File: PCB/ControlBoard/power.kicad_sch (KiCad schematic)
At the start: 26 parts, among them J10 BUSPWR, U5 TPS629210, U6 TPS629210

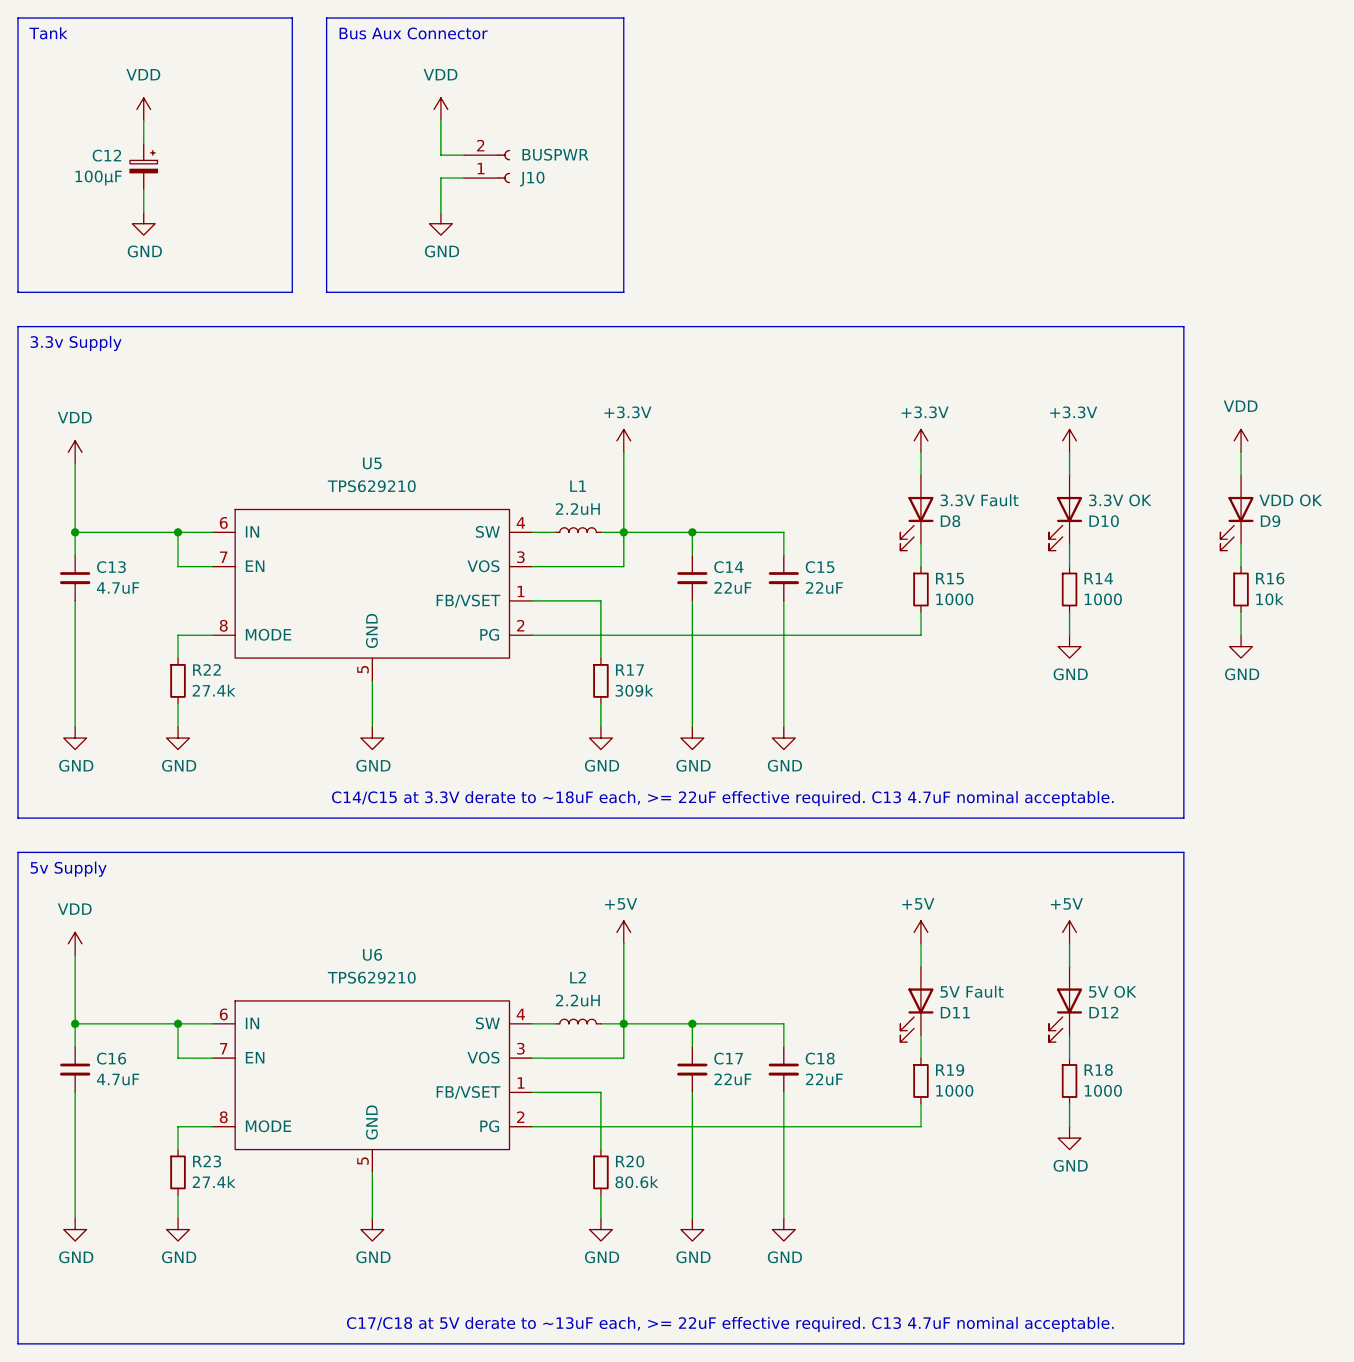
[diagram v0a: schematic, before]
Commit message: feat: Rework ControlBoard to use an STM32H562VGT6.
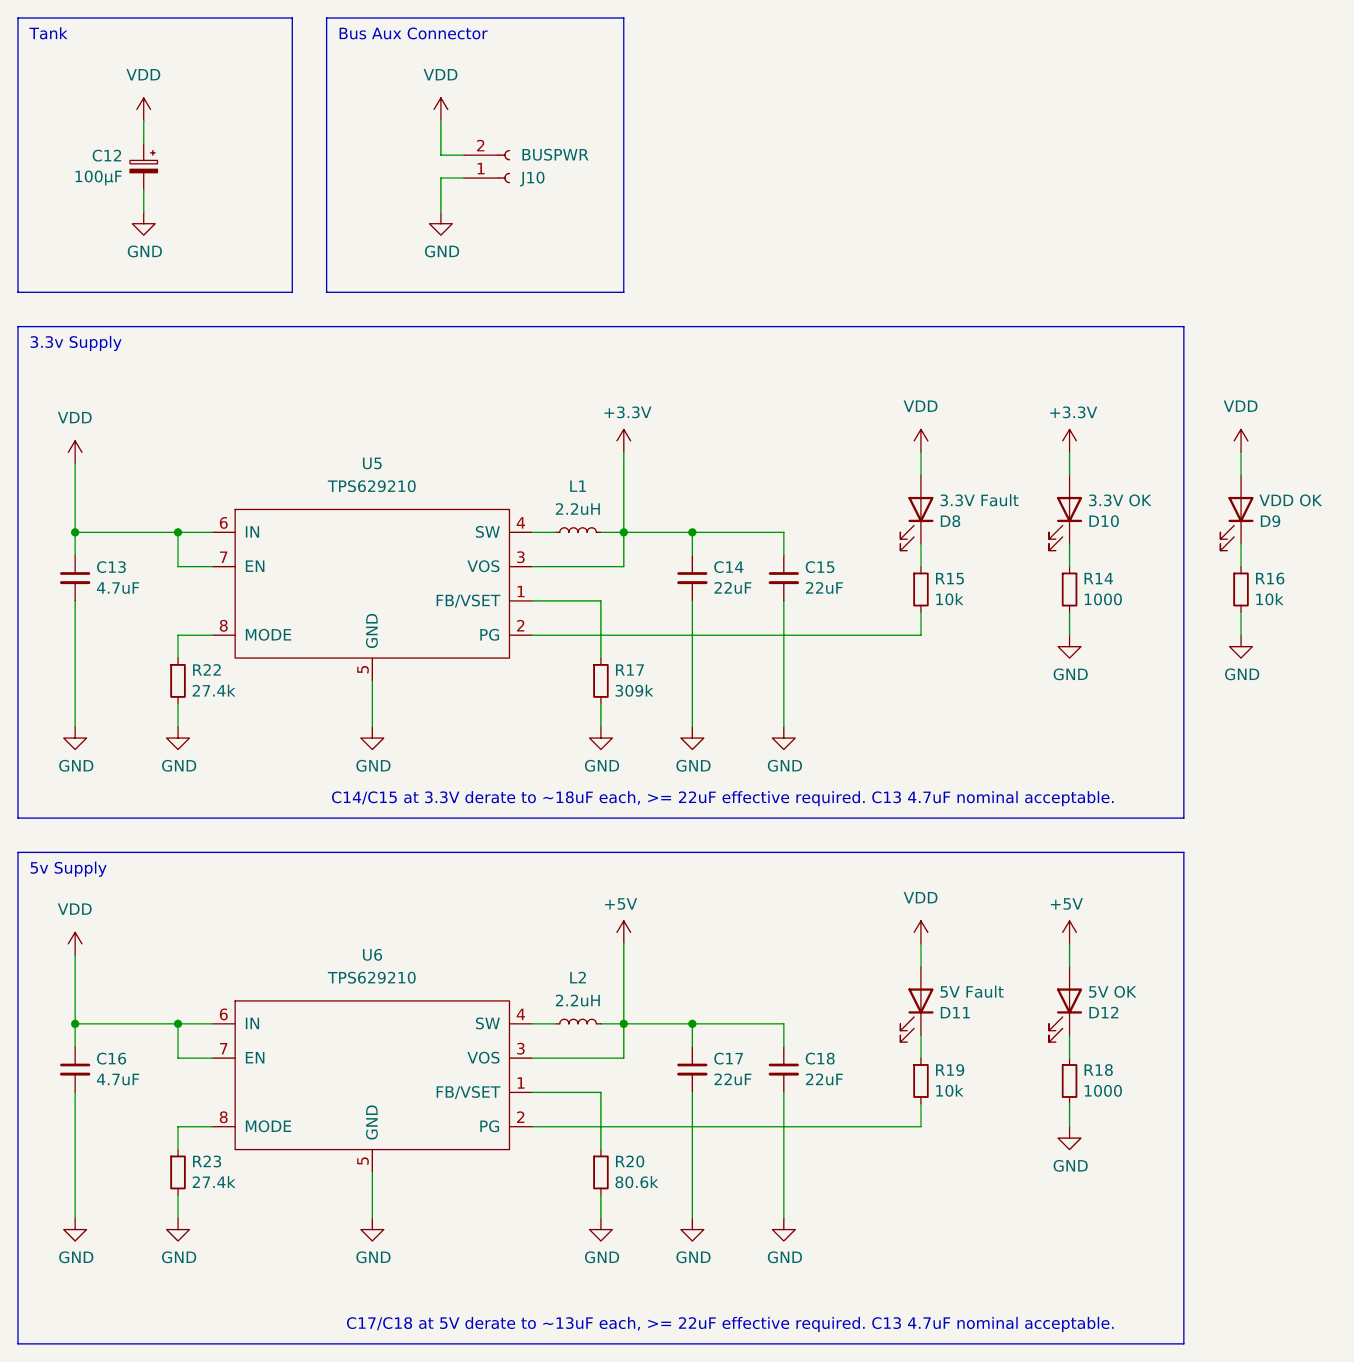
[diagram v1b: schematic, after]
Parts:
- R15, R19: value 1000 -> 10k; DIGIKEY P1.00KHCT-ND -> P10.0KHCT-ND
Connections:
- net +3.3V: no longer D8.2 (A)
- net +5V: no longer D11.2 (A)
- net VDD: now also D11.2 (A), D8.2 (A)
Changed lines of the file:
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@@
 			)
 		)
-		(property "Value" "1000"
+		(property "Value" "10k"
 			(at 117.0686 79.883 0)
 			(show_name no)
@@
 			)
 		)
-		(property "DIGIKEY" "P1.00KHCT-ND"
+		(property "DIGIKEY" "P10.0KHCT-ND"
 			(at 115.57 78.74 0)
 			(hide yes)
@@
 	)
 	(symbol
+		(lib_id "power:VDD")
+		(at 115.57 63.5 0)
+		(unit 1)
+		(body_style 1)
+		(exclude_from_sim no)
+		(in_bom yes)
+		(on_board yes)
+		(in_pos_files yes)
+		(dnp no)
+		(fields_autoplaced yes)
+		(property "Reference" "#PWR086"
+			(at 115.57 67.31 0)
+			(hide yes)
+			(show_name no)
+			(do_not_autoplace no)
+			(effects
+				(font
+					(size 1.27 1.27)
+				)
+			)
+		)
+		(property "Value" "VDD"
+			(at 115.57 58.42 0)
+			(show_name no)
+			(do_not_autoplace no)
+			(effects
+				(font
+					(size 1.27 1.27)
+				)
+			)
+		)
+		(property "Footprint" ""
+			(at 115.57 63.5 0)
+			(hide yes)
+			(show_name no)
+			(do_not_autoplace no)
+			(effects
+				(font
+					(size 1.27 1.27)
+				)
+			)
+		)
+		(property "Datasheet" ""
+			(at 115.57 63.5 0)
+			(hide yes)
+			(show_name no)
+			(do_not_autoplace no)
+			(effects
+				(font
+					(size 1.27 1.27)
+				)
+			)
+		)
+		(property "Description" "Power symbol creates a global label with name \"VDD\""
+			(at 115.57 63.5 0)
+			(hide yes)
+			(show_name no)
+			(do_not_autoplace no)
+			(effects
+				(font
+					(size 1.27 1.27)
+				)
+			)
+		)
+		(pin "1"
+		)
+		(instances
+			(project "ControlBoard"
+				(path "/8a650ebf-3f78-4ca4-a26b-a5028693e36d/8aac65e2-4dfd-463b-a6c0-b675e1c87ded"
+					(reference "#PWR086")
+					(unit 1)
+				)
+			)
+		)
+	)
+	(symbol
 		(lib_id "Device:C_Polarized_Small")
 		(at 29.21 31.75 0)
@@
 			)
 		)
-		(property "Value" "1000"
+		(property "Value" "10k"
 			(at 117.0686 134.493 0)
 			(show_name no)
@@
 			)
 		)
-		(property "DIGIKEY" "P1.00KHCT-ND"
+		(property "DIGIKEY" "P10.0KHCT-ND"
 			(at 115.57 133.35 0)
 			(hide yes)
@@
 	)
 	(symbol
-		(lib_id "power:+5V")
-		(at 115.57 118.11 0)
-		(mirror y)
-		(unit 1)
-		(body_style 1)
-		(exclude_from_sim no)
-		(in_bom yes)
-		(on_board yes)
-		(in_pos_files yes)
-		(dnp no)
-		(property "Reference" "#PWR086"
-			(at 115.57 121.92 0)
-			(hide yes)
-			(show_name no)
-			(do_not_autoplace no)
-			(effects
-				(font
-					(size 1.27 1.27)
-				)
-			)
-		)
-		(property "Value" "+5V"
-			(at 115.189 113.7158 0)
-			(show_name no)
-			(do_not_autoplace no)
-			(effects
-				(font
-					(size 1.27 1.27)
-				)
-			)
-		)
-		(property "Footprint" ""
-			(at 115.57 118.11 0)
-			(hide yes)
-			(show_name no)
-			(do_not_autoplace no)
-			(effects
-				(font
-					(size 1.27 1.27)
-				)
-			)
-		)
-		(property "Datasheet" ""
-			(at 115.57 118.11 0)
-			(hide yes)
-			(show_name no)
-			(do_not_autoplace no)
-			(effects
-				(font
-					(size 1.27 1.27)
-				)
-			)
-		)
-		(property "Description" "Power symbol creates a global label with name \"+5V\""
-			(at 115.57 118.11 0)
-			(hide yes)
-			(show_name no)
-			(do_not_autoplace no)
-			(effects
-				(font
-					(size 1.27 1.27)
-				)
-			)
-		)
-		(pin "1"
-		)
-		(instances
-			(project "ControlBoard"
-				(path "/8a650ebf-3f78-4ca4-a26b-a5028693e36d/8aac65e2-4dfd-463b-a6c0-b675e1c87ded"
-					(reference "#PWR086")
-					(unit 1)
-				)
-			)
-		)
-	)
-	(symbol
 		(lib_id "power:GND")
 		(at 132.08 83.82 0)
@@
 	)
 	(symbol
-		(lib_id "power:+3.3V")
-		(at 115.57 63.5 0)
-		(unit 1)
-		(body_style 1)
-		(exclude_from_sim no)
-		(in_bom yes)
-		(on_board yes)
-		(in_pos_files yes)
-		(dnp no)
-		(property "Reference" "#PWR073"
-			(at 115.57 67.31 0)
-			(hide yes)
-			(show_name no)
-			(do_not_autoplace no)
-			(effects
-				(font
-					(size 1.27 1.27)
-				)
-			)
-		)
-		(property "Value" "+3.3V"
-			(at 115.951 59.1058 0)
-			(show_name no)
-			(do_not_autoplace no)
-			(effects
-				(font
-					(size 1.27 1.27)
-				)
-			)
-		)
-		(property "Footprint" ""
-			(at 115.57 63.5 0)
-			(hide yes)
-			(show_name no)
-			(do_not_autoplace no)
-			(effects
-				(font
-					(size 1.27 1.27)
-				)
-			)
-		)
-		(property "Datasheet" ""
-			(at 115.57 63.5 0)
-			(hide yes)
-			(show_name no)
-			(do_not_autoplace no)
-			(effects
-				(font
-					(size 1.27 1.27)
-				)
-			)
-		)
-		(property "Description" "Power symbol creates a global label with name \"+3.3V\""
-			(at 115.57 63.5 0)
-			(hide yes)
-			(show_name no)
-			(do_not_autoplace no)
-			(effects
-				(font
-					(size 1.27 1.27)
-				)
-			)
-		)
-		(pin "1"
-		)
-		(instances
-			(project "ControlBoard"
-				(path "/8a650ebf-3f78-4ca4-a26b-a5028693e36d/8aac65e2-4dfd-463b-a6c0-b675e1c87ded"
-					(reference "#PWR073")
-					(unit 1)
-				)
-			)
-		)
-	)
-	(symbol
 		(lib_id "power:GND")
 		(at 21.59 148.59 0)
@@
 					(unit 1)
 				)
+			)
+		)
+	)
+	(symbol
+		(lib_id "power:VDD")
+		(at 115.57 118.11 0)
+		(unit 1)
+		(body_style 1)
+		(exclude_from_sim no)
+		(in_bom yes)
+		(on_board yes)
+		(in_pos_files yes)
+		(dnp no)
+		(fields_autoplaced yes)
+		(property "Reference" "#PWR097"
+			(at 115.57 121.92 0)
+			(hide yes)
+			(show_name no)
+			(do_not_autoplace no)
+			(effects
+				(font
+					(size 1.27 1.27)
+				)
+			)
+		)
+		(property "Value" "VDD"
+			(at 115.57 113.03 0)
+			(show_name no)
+			(do_not_autoplace no)
+			(effects
+				(font
+					(size 1.27 1.27)
+				)
+			)
+		)
+		(property "Footprint" ""
+			(at 115.57 118.11 0)
+			(hide yes)
+			(show_name no)
+			(do_not_autoplace no)
+			(effects
+				(font
+					(size 1.27 1.27)
+				)
+			)
+		)
+		(property "Datasheet" ""
+			(at 115.57 118.11 0)
+			(hide yes)
+			(show_name no)
+			(do_not_autoplace no)
+			(effects
+				(font
+					(size 1.27 1.27)
+				)
+			)
+		)
+		(property "Description" "Power symbol creates a global label with name \"VDD\""
+			(at 115.57 118.11 0)
+			(hide yes)
+			(show_name no)
+			(do_not_autoplace no)
+			(effects
+				(font
+					(size 1.27 1.27)
+				)
+			)
+		)
+		(pin "1"
+		)
+		(instances
+			(project "ControlBoard"
+				(path "/8a650ebf-3f78-4ca4-a26b-a5028693e36d/8aac65e2-4dfd-463b-a6c0-b675e1c87ded"
+					(reference "#PWR097")
+					(unit 1)
+				)
